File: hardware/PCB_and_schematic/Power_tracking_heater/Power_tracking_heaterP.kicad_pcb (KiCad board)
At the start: 2 copper layers, 99.5 x 99.5 mm, 65 parts, among them J2 DISPLAY, J3 DS18B20, J4 PROG_INTERFACE, J5 Screw_Terminal_01x05, J6 USER_PANEL, Q1 BC807, Q2 BC807, Q3 BC817, Q4 BC817, Q5 BC817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

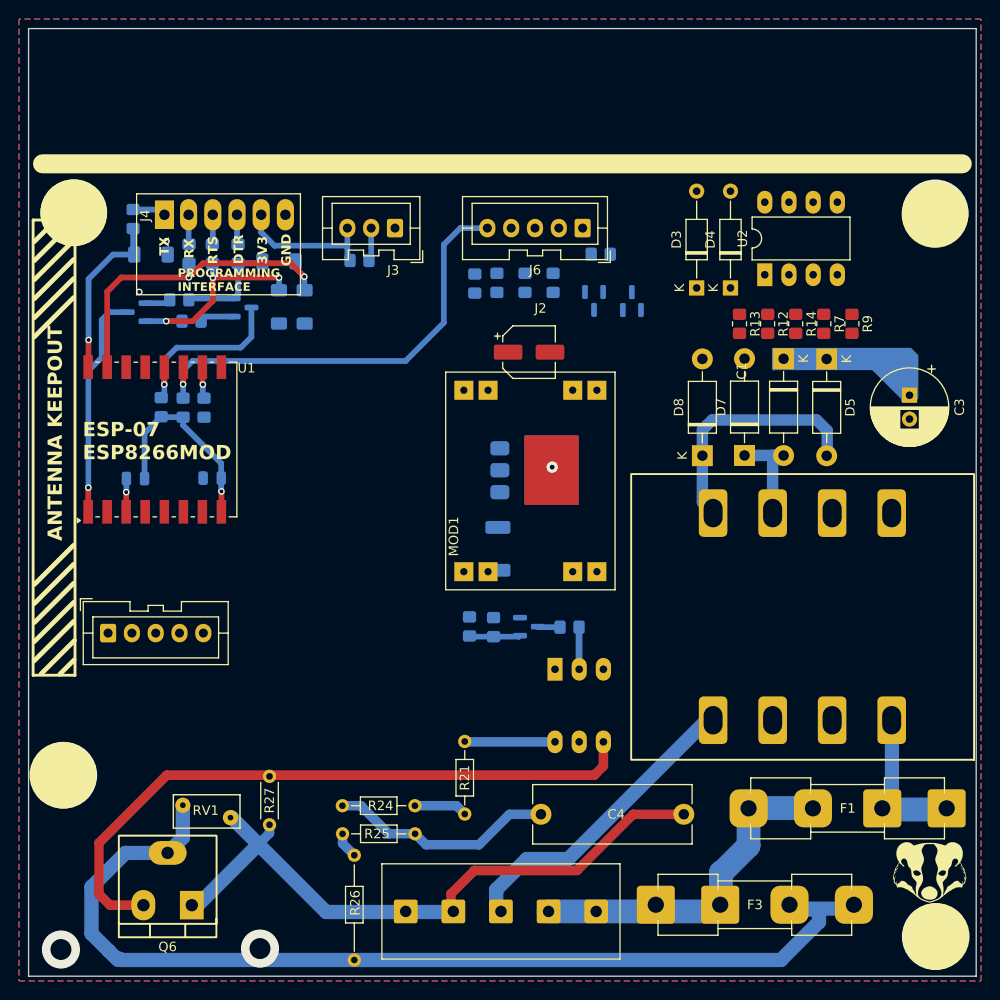
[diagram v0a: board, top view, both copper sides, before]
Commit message: update of power tracking heater
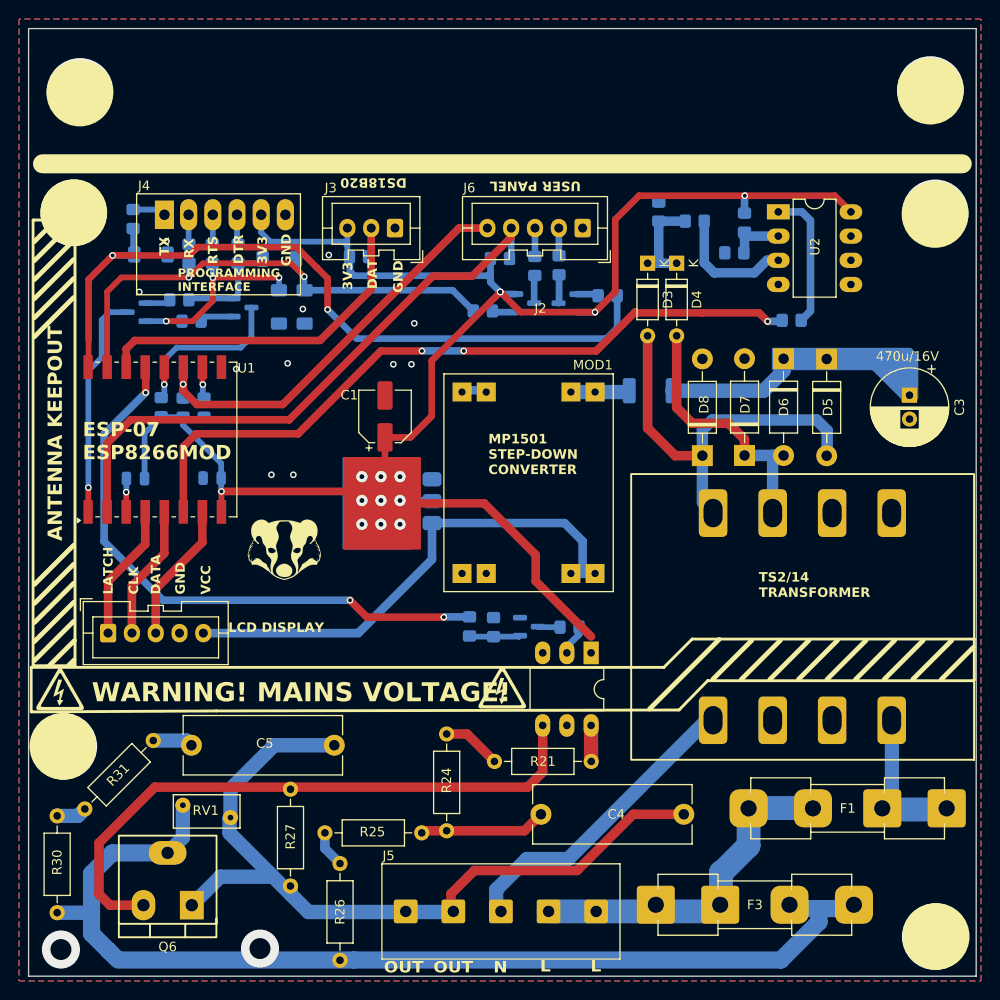
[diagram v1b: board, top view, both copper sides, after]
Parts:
- added C5: 10n/250V, Capacitor_THT:C_Rect_L16.5mm_W6.0mm_P15.00mm_MKT, F.Cu at (121.4, 110.4)
- added G***: LOGO, My-Footprints:high-voltage, F.Cu at (107.6, 104.5)
- added G***: LOGO, My-Footprints:high-voltage, F.Cu at (154.0, 104.3)
- added G***: LOGO, My-Footprints:high-voltage, B.Cu at (154.0, 104.4)
- added G***: LOGO, My-Footprints:high-voltage, B.Cu at (107.5, 104.4)
- added R30: 50R, Resistor_THT:R_Axial_DIN0207_L6.3mm_D2.5mm_P10.16mm_Horizontal, F.Cu at (107.3, 128.0)
- added R31: 50R, Resistor_THT:R_Axial_DIN0207_L6.3mm_D2.5mm_P10.16mm_Horizontal, F.Cu at (110.2, 117.1)
- D3, D4: footprint Diode_THT:D_DO-35_SOD27_P10.16mm_Horizontal -> Diode_THT:D_DO-35_SOD27_P7.62mm_Horizontal
- R12, R13, R14, R7, R9: moved to B.Cu
- R21, R24, R25, R26: footprint Resistor_THT:R_Axial_DIN0204_L3.6mm_D1.6mm_P7.62mm_Horizontal -> Resistor_THT:R_Axial_DIN0207_L6.3mm_D2.5mm_P10.16mm_Horizontal
- R27: value 390R -> ~; footprint Resistor_THT:R_Axial_DIN0204_L3.6mm_D1.6mm_P5.08mm_Horizontal -> Resistor_THT:R_Axial_DIN0207_L6.3mm_D2.5mm_P10.16mm_Horizontal
- U4: moved to F.Cu
- moved G*** 75.7 mm to (131.2, 89.9)
- moved MOD1 28.7 mm to (165.7, 71.4), turned to -90 degrees
- moved F2 23.1 mm to (169.6, 73.2), turned to 180 degrees
- moved R7 21.0 mm to (170.5, 54.4), turned to 90 degrees
- moved R9 19.7 mm to (174.2, 55.4), turned to 180 degrees
- moved C1 16.6 mm to (141.7, 75.9), turned to 90 degrees
- moved U3 13.8 mm to (143.5, 84.8), turned to 180 degrees
- moved R24 11.3 mm to (148.2, 119.4), turned to 90 degrees
- moved R12 10.9 mm to (179.5, 55.5)
- moved R13 7.47 mm to (178.4, 58.7), turned to 180 degrees
- moved Q2 7.23 mm to (156.4, 64.0), turned to 0 degrees
- moved Q1 6.77 mm to (160.9, 64.0), turned to 180 degrees
- moved U2 6.75 mm to (183.0, 54.4), turned to 0 degrees
- moved R21 6.35 mm to (153.2, 112.1), turned to 0 degrees
- moved D4 6.22 mm to (172.3, 59.8), turned to -90 degrees
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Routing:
- net +3V3: track 36.3 -> 188.9 mm, vias 2 -> 14
- net ZERO_CROSSING_SIGNAL: track 0.00 -> 76.0 mm, vias 0 -> 3
- net TXD: track 17.9 -> 81.0 mm, vias 1 -> 2
- net PUSH_BUTTON_2: track 0.00 -> 62.8 mm
- net AC_POWER_DRIVE: track 0.00 -> 61.8 mm, vias 0 -> 3
- net +5V: track 0.00 -> 53.6 mm
- net DS18B20: track 3.51 -> 40.2 mm
- net RXD: track 33.4 -> 52.0 mm
- net AC_SEC_2: track 12.1 -> 29.8 mm
- net AC_SEC_1: track 25.9 -> 42.5 mm
- net Net-(J5-Pin_4): track 69.0 -> 84.8 mm
- net MOSI: track 0.00 -> 14.8 mm
- net Net-(R14-Pad2): track 0.00 -> 14.6 mm
- net CS: track 0.00 -> 14.3 mm
- net CLK: track 0.00 -> 14.1 mm
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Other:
- board text added: "470u/16V"
- board text added: "CLK"
- board text added: "DAT"
- board text added: "DATA"
- board text added: "DS18B20"
- board text added: "L"
- board text added: "LATCH"
- board text added: "LCD DISPLAY"
- board text added: "MP1501 STEP-DOWN CONVERTER"
- board text added: "N"
- board text added: "OUT"
- board text added: "TS2/14 TRANSFORMER"
- board text added: "USER PANEL"
- board text added: "VCC"
- board text added: "WARNING! MAINS VOLTAGE!"

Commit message: Power tracking heater done
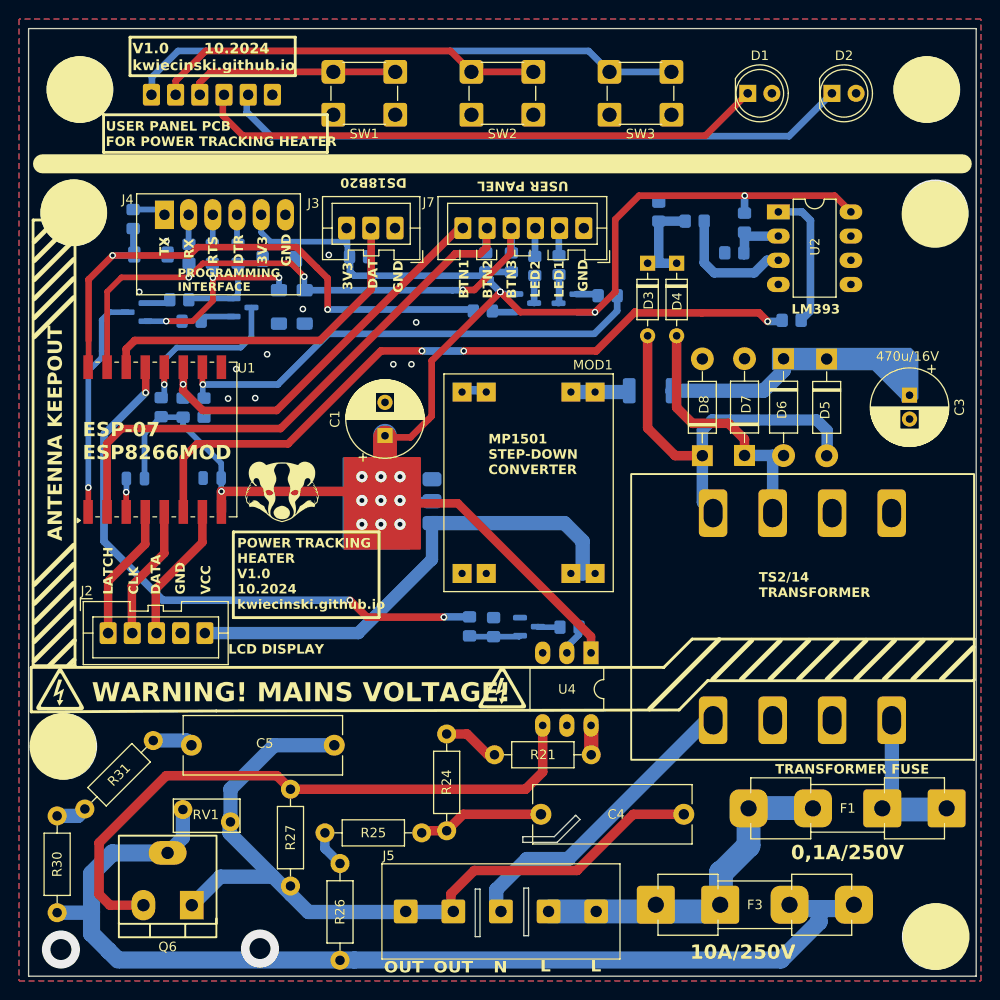
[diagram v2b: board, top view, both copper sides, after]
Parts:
- removed J6: USER_PANEL, Connector_JST:JST_XA_B05B-XASK-1_1x05_P2.50mm_Vertical
- added D1: LED, LED_THT:LED_D5.0mm, F.Cu at (179.8, 42.0)
- added D2: LED, LED_THT:LED_D5.0mm, F.Cu at (188.7, 42.0)
- added J1: USER_PANEL, My-Footprints-connectors:JST_XH_1x06_P2.54mm_Vertical, B.Cu at (129.7, 42.1)
- added J7: USER_PANEL, My-Footprints-connectors:JST_XH_1x06_P2.54mm_Vertical, F.Cu at (162.4, 56.1)
- added R32: 10k, Resistor_SMD:R_0805_2012Metric_Pad1.20x1.40mm_HandSolder, B.Cu at (155.0, 59.7)
- added SW1: SW_Push, My-Footprints:SW_PUSH_6mm, F.Cu at (142.8, 44.2)
- added SW2: SW_Push, My-Footprints:SW_PUSH_6mm, F.Cu at (157.3, 44.2)
- added SW3: SW_Push, My-Footprints:SW_PUSH_6mm, F.Cu at (171.8, 44.2)
- C1: footprint Capacitor_SMD:CP_Elec_5x5.7 -> Capacitor_THT:CP_Radial_D8.0mm_P3.50mm
- D5, D6, D7, D8: footprint Diode_THT:D_DO-41_SOD81_P10.16mm_Horizontal -> My-Footprints:DO-41_SOD81_P10.16mm_Horizontal
- F1: value Fuse -> 100mA/250V
- F3: value Fuse -> 10A/250V
- J2: footprint Connector_JST:JST_XA_B05B-XASK-1_1x05_P2.50mm_Vertical -> My-Footprints:JST_XA_1x05_P2.50mm_Vertical
- J3: footprint Connector_JST:JST_XA_B03B-XASK-1_1x03_P2.50mm_Vertical -> My-Footprints-connectors:JST_XA_1x03_P2.54mm_Vertical
- J5: value Screw_Terminal_01x05 -> POWER_OUTPUT
- R21, R24, R25, R26, R27, R30, R31: footprint Resistor_THT:R_Axial_DIN0207_L6.3mm_D2.5mm_P10.16mm_Horizontal -> My-Footprints:R_Axial_DIN0207_L6.3mm_D2.5mm_P10.16mm_Horizontal
- moved G*** 6.08 mm to (130.9, 83.8)
- moved C1 2.03 mm to (141.7, 77.9)
- moved R3 1.55 mm to (152.3, 59.7), turned to -90 degrees
- moved R21 0.70 mm to (153.2, 111.4)
- moved RV1 0.45 mm to (125.5, 118.5)
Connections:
- D11 pad 1: TXD -> TXD_LED2
- D12 pad 1: RXD -> RXD_PUSH_BUTTON_3
- R1 pad 2: TXD -> LED_1
- R2 pad 2: RXD -> TXD_LED2
- R28 pad 1: TXD -> TXD_LED2
- R29 pad 1: RXD -> RXD_PUSH_BUTTON_3
- R4 pad 1: LED_1 -> LED_1_OUT
- R5 pad 1: LED_2 -> LED_2_OUT
- R8 pad 1: Net-(U1-GPIO15) -> LED_1
- U1 pad 10: Net-(U1-GPIO15) -> LED_1
- U1 pad 15: RXD -> RXD_PUSH_BUTTON_3
- U1 pad 16: TXD -> TXD_LED2
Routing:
- net TXD: track 81.0 -> 0.00 mm, vias 2 -> 0
- net Net-(D2-A): track 0.00 -> 66.3 mm
- net RXD_PUSH_BUTTON_3: track 0.00 -> 61.9 mm, vias 0 -> 3
- net TXD_LED2: track 0.00 -> 60.8 mm, vias 0 -> 2
- net Net-(D1-A): track 0.00 -> 60.0 mm
- net Net-(J1-Pin_6): track 0.00 -> 58.3 mm
- net RXD: track 52.0 -> 0.00 mm, vias 2 -> 0
- net LED_1: track 2.91 -> 51.6 mm, vias 0 -> 1
- net Net-(J1-Pin_5): track 0.00 -> 41.1 mm
- net Net-(J1-Pin_4): track 0.00 -> 22.1 mm
- net +3V3: track 188.9 -> 194.1 mm
- net Net-(U1-GPIO15): track 3.32 -> 0.00 mm, vias 1 -> 0
- net LED_2_OUT: track 0.00 -> 2.99 mm
- net LED_2: track 2.99 -> 0.00 mm
- net LED_1_OUT: track 0.00 -> 2.91 mm
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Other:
- outline, holes or cut-outs redrawn
- board text added: "0,1A/250V"
- board text added: "10A/250V"
- board text added: "300mA"
- board text added: "BTN1"
- board text added: "BTN2"
- board text added: "BTN3"
- board text added: "LED1"
- board text added: "LED2"
- board text added: "LM393"
- board text added: "POWER TRACKING HEATER V1.0 10.2024 kwiecinski.github.io"
- board text added: "TRANSFORMER FUSE"
- board text added: "USER PANEL PCB FOR POWER TRACKING HEATER"
- board text added: "V1.0 10.2024 kwiecinski.github.io"
